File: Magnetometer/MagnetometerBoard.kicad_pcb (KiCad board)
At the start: 2 copper layers, 39.5 x 82.5 mm, 4 parts, among them J1 Conn_01x04_Socket, J2 Conn_01x04_Socket

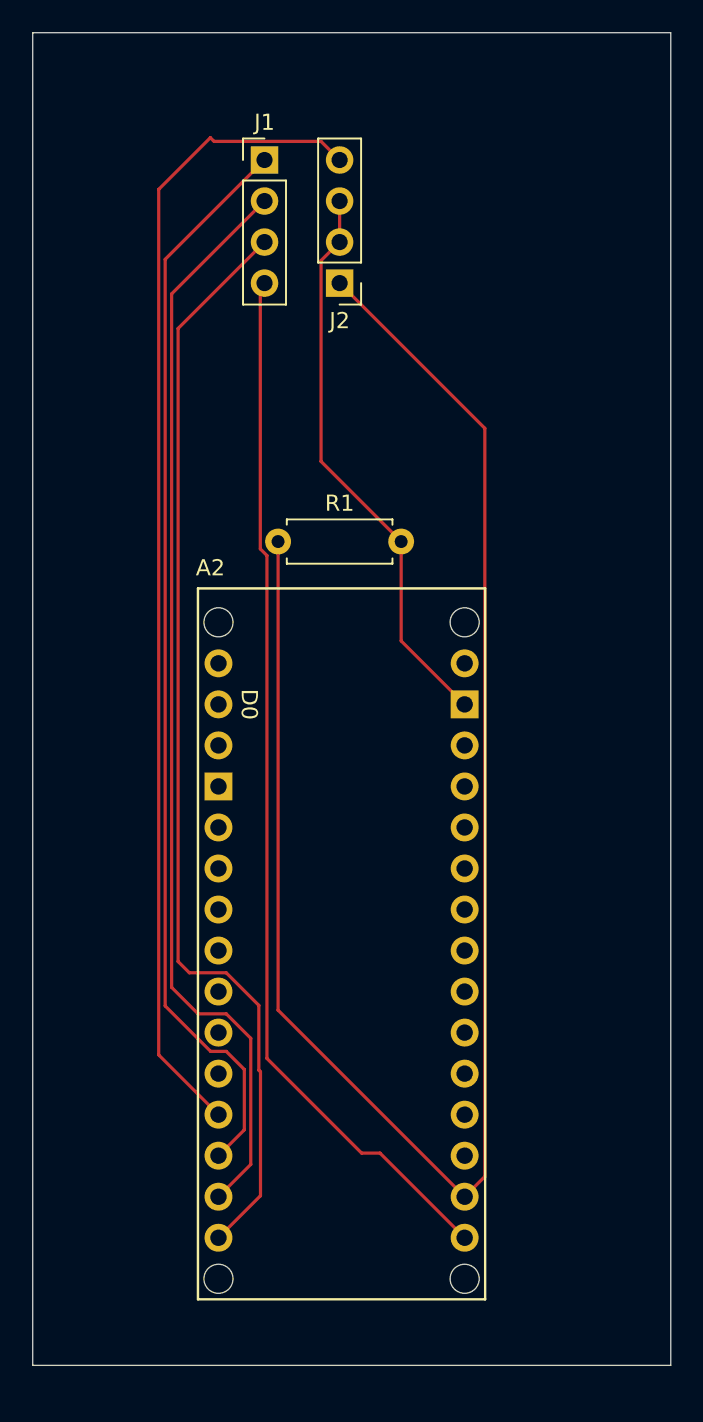
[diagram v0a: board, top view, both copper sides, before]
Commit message: finailzied prototype for the magnetometer pcb
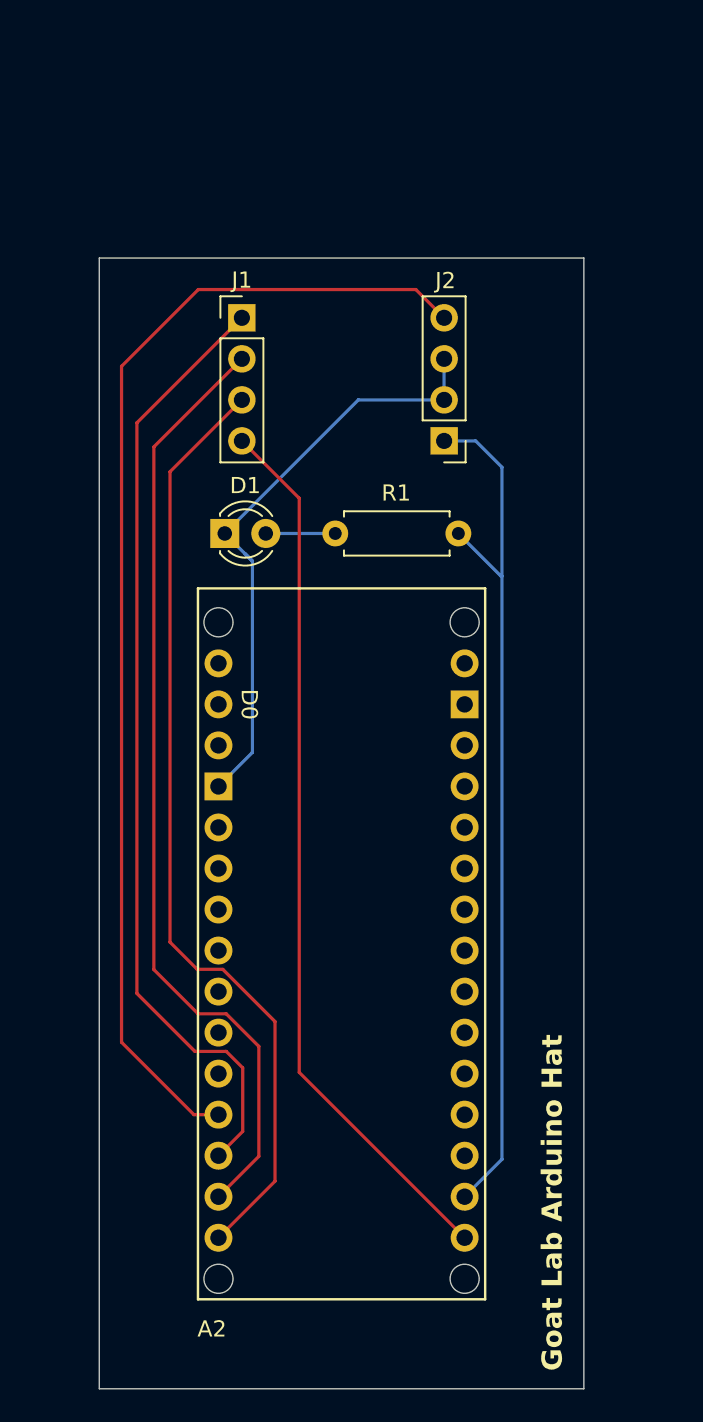
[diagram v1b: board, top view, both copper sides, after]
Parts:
- added D1: GREEN LED, LED_THT:LED_D3.0mm, F.Cu at (104.9, 65.0)
- moved J2 11.7 mm to (118.5, 59.3)
- moved R1 11.2 mm to (119.3, 65.0), turned to 180 degrees
- moved J1 9.87 mm to (106.0, 51.6)
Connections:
- R1 pad 1: +3.3V -> Net-(D1-K)
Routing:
- net +3.3V: track 106.1 -> 58.5 mm
- net /CLK: track 65.1 -> 55.0 mm
- net /MISO: track 68.4 -> 58.8 mm
- net /MOSI: track 67.9 -> 58.9 mm
- net /SSN: track 67.4 -> 59.0 mm
- net GND: track 35.3 -> 37.5 mm
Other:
- board size 39.5 x 82.5 mm -> 30 x 70 mm
- board text added: "Goat Lab Arduino Hat"

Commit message: added logo + title
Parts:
- added G***: LOGO, IrishSat_Logo:even-mini_er-Logo, F.Cu at (123.3, 54.2)
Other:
- board text added: "Goat Lab Magnetometer"
- board text removed: "Goat Lab Arduino Hat"
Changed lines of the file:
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@@
+		)
+	)
+	(footprint "IrishSat_Logo:even-mini_er-Logo"
+		(layer "F.Cu")
+		(at 123.3 54.2)
+		(property "Reference" "G***"
+			(at 0 0 0)
+			(layer "F.SilkS")
+			(hide yes)
+			(effects
+				(font
+					(size 1.5 1.5)
+					(thickness 0.3)
+				)
+			)
+		)
+		(property "Value" "LOGO"
+			(at 0.75 0 0)
+			(layer "F.SilkS")
+			(hide yes)
+			(effects
+				(font
+					(size 1.5 1.5)
+					(thickness 0.3)
+				)
+			)
+		)
+		(property "Footprint" "IrishSat_Logo:even-mini_er-Logo"
+			(at 0 0 0)
+			(layer "F.Fab")
+			(hide yes)
+			(effects
+				(font
+					(size 1.27 1.27)
+					(thickness 0.15)
+				)
+			)
+		)
+		(property "Datasheet" ""
+			(at 0 0 0)
+			(layer "F.Fab")
+			(hide yes)
+			(effects
+				(font
+					(size 1.27 1.27)
+					(thickness 0.15)
+				)
+			)
+		)
+		(property "Description" ""
+			(at 0 0 0)
+			(layer "F.Fab")
+			(hide yes)
+			(effects
+				(font
+					(size 1.27 1.27)
+					(thickness 0.15)
+				)
+			)
+		)
+		(attr board_only exclude_from_pos_files exclude_from_bom)
+		(fp_poly
+			(pts
+				(xy 0.020289 0.821393) (xy -0.019588 0.861286) (xy -0.090582 0.924465) (xy -0.184797 1.004189) (xy -0.294339 1.093717)
+				(xy -0.411313 1.186307) (xy -0.527824 1.275219) (xy -0.589805 1.320803) (xy -0.818653 1.472996)
+				(xy -1.078808 1.623975) (xy -1.350622 1.763846) (xy -1.614452 1.882716) (xy -1.850652 1.970693)
+				(xy -1.92354 1.99246) (xy -2.143783 2.039015) (xy -2.366045 2.061708) (xy -2.57201 2.060327) (xy -2.743362 2.034661)
+				(xy -2.831398 2.002907) (xy -2.980549 1.892108) (xy -3.072562 1.743717) (xy -3.105848 1.562693)
+				(xy -3.078819 1.353994) (xy -3.059813 1.290028) (xy -2.99767 1.102934) (xy -2.935733 1.248772) (xy -2.864477 1.372418)
+				(xy -2.763632 1.461244) (xy -2.618705 1.525036) (xy -2.471034 1.562617) (xy -2.273527 1.582097)
+				(xy -2.030688 1.57164) (xy -1.759307 1.533516) (xy -1.476174 1.469993) (xy -1.231056 1.395034) (xy -1.068016 1.333528)
+				(xy -0.873933 1.253003) (xy -0.665254 1.16105) (xy -0.458427 1.065259) (xy -0.2699 0.97322) (xy -0.11612 0.892522)
+				(xy -0.024883 0.83843) (xy 0.021156 0.811527)
+			)
+			(stroke
+				(width 0)
+				(type solid)
+			)
+			(fill solid)
+			(layer "F.SilkS")
+		)
+		(fp_poly
+			(pts
+				(xy 2.790229 -2.907449) (xy 2.823565 -2.821815) (xy 2.867584 -2.694761) (xy 2.917642 -2.539108)
+				(xy 2.921165 -2.527754) (xy 2.976418 -2.3497) (xy 3.02974 -2.178614) (xy 3.074647 -2.035259) (xy 3.102157 -1.948215)
+				(xy 3.129936 -1.849077) (xy 3.141936 -1.78065) (xy 3.139735 -1.76361) (xy 3.103182 -1.748792) (xy 3.013173 -1.71784)
+				(xy 2.883191 -1.67501) (xy 2.726715 -1.624559) (xy 2.557226 -1.570741) (xy 2.388206 -1.517814) (xy 2.233134 -1.470033)
+				(xy 2.105491 -1.431655) (xy 2.018759 -1.406936) (xy 1.987533 -1.399841) (xy 1.949667 -1.424134)
+				(xy 1.94876 -1.425688) (xy 1.923477 -1.48743) (xy 1.887087 -1.597144) (xy 1.843268 -1.741344) (xy 1.7957 -1.906543)
+				(xy 1.748063 -2.079257) (xy 1.704034 -2.246) (xy 1.667294 -2.393286) (xy 1.641522 -2.507629) (xy 1.630396 -2.575543)
+				(xy 1.631648 -2.58806) (xy 1.671324 -2.604916) (xy 1.764374 -2.637105) (xy 1.896991 -2.680382) (xy 2.055372 -2.7305)
+				(xy 2.225713 -2.783215) (xy 2.394208 -2.834281) (xy 2.547053 -2.879452) (xy 2.670444 -2.914483)
+				(xy 2.750575 -2.935127) (xy 2.772222 -2.938843)
+			)
+			(stroke
+				(width 0)
+				(type solid)
+			)
+			(fill solid)
+			(layer "F.SilkS")
+		)
+		(fp_poly
+			(pts
+				(xy 0.153152 -1.624227) (xy 0.323587 -1.61521) (xy 0.458455 -1.598133) (xy 0.574881 -1.571316) (xy 0.612258 -1.560016)
+				(xy 0.983705 -1.406406) (xy 1.315619 -1.196324) (xy 1.604476 -0.93329) (xy 1.846756 -0.620824) (xy 2.038937 -0.26245)
+				(xy 2.120167 -0.052479) (xy 2.164084 0.087068) (xy 2.192208 0.209994) (xy 2.207857 0.340116) (xy 2.214352 0.501251)
+				(xy 2.215237 0.629752) (xy 2.212812 0.822775) (xy 2.203324 0.969747) (xy 2.183454 1.09449) (xy 2.149884 1.220826)
+				(xy 2.120198 1.311984) (xy 1.957068 1.690715) (xy 1.741172 2.027287) (xy 1.476907 2.317475) (xy 1.168667 2.557055)
+				(xy 0.82085 2.741802) (xy 0.524793 2.845153) (xy 0.315655 2.888046) (xy 0.075908 2.913883) (xy -0.162851 2.920586)
+				(xy -0.369028 2.906076) (xy -0.378935 2.9046) (xy -0.659784 2.842413) (xy -0.939595 2.74672) (xy -1.189429 2.628057)
+				(xy -1.267219 2.581252) (xy -1.479423 2.444098) (xy -1.273252 2.321313) (xy -0.67943 1.940604) (xy -0.152004 1.544783)
+				(xy 0.311404 1.131638) (xy 0.713172 0.698956) (xy 1.055676 0.244524) (xy 1.197566 0.021618) (xy 1.293688 -0.145247)
+				(xy 1.348284 -0.257469) (xy 1.361687 -0.316476) (xy 1.33423 -0.323697) (xy 1.26825 -0.2821) (xy 0.896967 -0.025426)
+				(xy 0.472121 0.220396) (xy 0.010072 0.447144) (xy -0.472821 0.646593) (xy -0.818592 0.766877) (xy -1.123068 0.857846)
+				(xy -1.414209 0.932533) (xy -1.681937 0.989105) (xy -1.916175 1.025727) (xy -2.106842 1.040566)
+				(xy -2.243862 1.031789) (xy -2.257659 1.028705) (xy -2.352053 1.005014) (xy -2.335801 0.563733)
+				(xy -2.325937 0.359015) (xy -2.311474 0.20319) (xy -2.289011 0.075187) (xy -2.255146 -0.046063)
+				(xy -2.222188 -0.139945) (xy -2.05395 -0.50583) (xy -1.836952 -0.823378) (xy -1.566294 -1.09877)
+				(xy -1.308994 -1.292122) (xy -1.086789 -1.425108) (xy -0.872598 -1.520037) (xy -0.647791 -1.581944)
+				(xy -0.393736 -1.615861) (xy -0.091805 -1.626821) (xy -0.069973 -1.626859)
+			)
+			(stroke
+				(width 0)
+				(type solid)
+			)
+			(fill solid)
+			(layer "F.SilkS")
 		)
 	)
@@
 		(layer "Edge.Cuts")
 	)
-	(gr_text "Goat Lab Arduino Hat"
+	(gr_text "Goat Lab Magnetometer"
 		(at 125.9 116.85 90)
 		(layer "F.SilkS")

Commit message: no trap
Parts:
- moved R1 2.55 mm to (121.9, 65.1)
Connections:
- R1 pad 1: Net-(D1-K) -> +3.3V
- R1 pad 2: GND -> +3.3V
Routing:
- net +3.3V: track 58.5 -> 57.1 mm
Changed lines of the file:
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@@
 	(footprint "Resistor_THT:R_Axial_DIN0207_L6.3mm_D2.5mm_P7.62mm_Horizontal"
 		(layer "F.Cu")
-		(at 119.35 65 180)
+		(at 121.9 65.1 180)
 		(descr "Resistor, Axial_DIN0207 series, Axial, Horizontal, pin pitch=7.62mm, 0.25W = 1/4W, length*diameter=6.3*2.5mm^2, http://cdn-reichelt.de/documents/datenblatt/B400/1_4W%23YAG.pdf")
 		(tags "Resistor Axial_DIN0207 series Axial Horizontal pin pitch 7.62mm 0.25W = 1/4W length 6.3mm diameter 2.5mm")
@@
 			(layers "*.Cu" "*.Mask")
 			(remove_unused_layers no)
-			(net 30 "Net-(D1-K)")
+			(net 25 "+3.3V")
 			(pintype "passive")
 		)
@@
 			(layers "*.Cu" "*.Mask")
 			(remove_unused_layers no)
-			(net 24 "GND")
+			(net 25 "+3.3V")
 			(pintype "passive")
 		)
@@
 	)
 	(segment
-		(start 107.43 65)
-		(end 111.73 65)
+		(start 121.9 60.75)
+		(end 120.42 59.27)
 		(width 0.2)
 		(layer "B.Cu")
@@
 	)
 	(segment
-		(start 122 67.65)
-		(end 122.05 67.65)
+		(start 121.9 65.1)
+		(end 121.9 103.9)
 		(width 0.2)
 		(layer "B.Cu")
@@
 	)
 	(segment
-		(start 122.05 103.75)
-		(end 119.74 106.06)
+		(start 121.9 65.1)
+		(end 121.9 60.75)
 		(width 0.2)
 		(layer "B.Cu")
@@
 	)
 	(segment
-		(start 122.05 60.9)
-		(end 122.05 67.65)
+		(start 107.43 65)
+		(end 107.53 65.1)
 		(width 0.2)
 		(layer "B.Cu")
@@
 	)
 	(segment
+		(start 121.9 103.9)
+		(end 119.74 106.06)
+		(width 0.2)
+		(layer "B.Cu")
+		(net 25)
+	)
+	(segment
+		(start 107.53 65.1)
+		(end 114.28 65.1)
+		(width 0.2)
+		(layer "B.Cu")
+		(net 25)
+	)
+	(segment
 		(start 118.47 59.27)
 		(end 120.42 59.27)
 		(width 0.2)
 		(layer "B.Cu")
-		(net 25)
-	)
-	(segment
-		(start 119.35 65)
-		(end 122 67.65)
-		(width 0.2)
-		(layer "B.Cu")
-		(net 25)
-	)
-	(segment
-		(start 122.05 67.65)
-		(end 122.05 103.75)
-		(width 0.2)
-		(layer "B.Cu")
-		(net 25)
-	)
-	(segment
-		(start 120.42 59.27)
-		(end 122.05 60.9)
-		(width 0.2)
-		(layer "B.Cu")
